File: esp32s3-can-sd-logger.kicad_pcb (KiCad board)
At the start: 4 copper layers, 84 x 72 mm, 162 parts, among them J1 PWR + CAN harness, J2 USB-C, J3 UART0, J4 I2C / Qwiic, J5 Spare IO, J6 Rail break-out, J7 microSD push-pull, J8 Sensor harness, Q1 100V 6.8mOhm N-ch, Q2 -20V 2.3A P-ch, Q3 60V 300mA N-ch, SW1 RESET, SW2 BOOT, U1 LM74700-Q1, U2 LM5164 (5V), U3 LM5164 (3V3), U4 ESP32-S3-WROOM-1-N16R8, U5 USBLC6-2SC6, U6 TJA1051T/3, U7 ADS1115

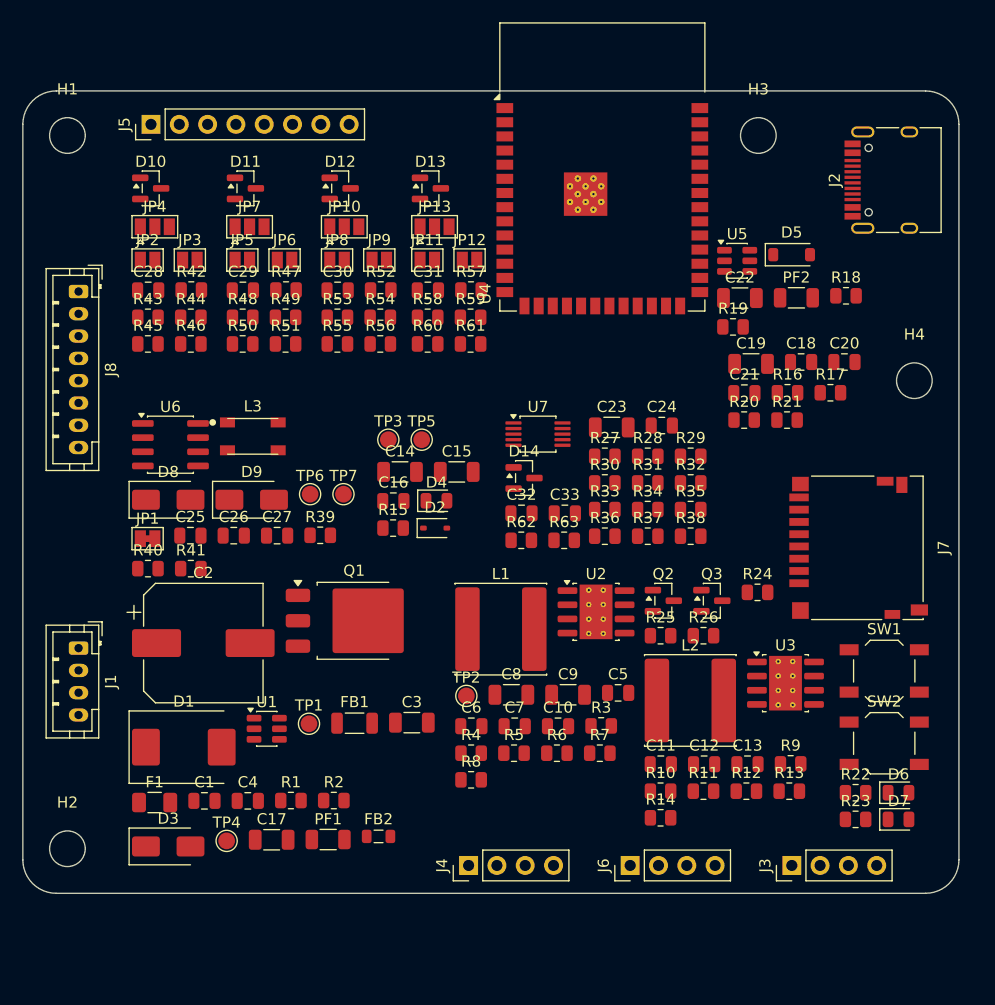
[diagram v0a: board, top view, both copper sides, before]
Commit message: Add WS2812 5V DIN, SPI breakout, and PCB handoff docs.
Shift-light header uses a 74AHCT1G125 so GPIO48 drives real 5V data; SPI lands on IO40/41/42/47 with spare IO3/45/46 kept. README §10 covers remaining routing for the next agent.

Co-authored-by: Cursor <cursoragent@cursor.com>
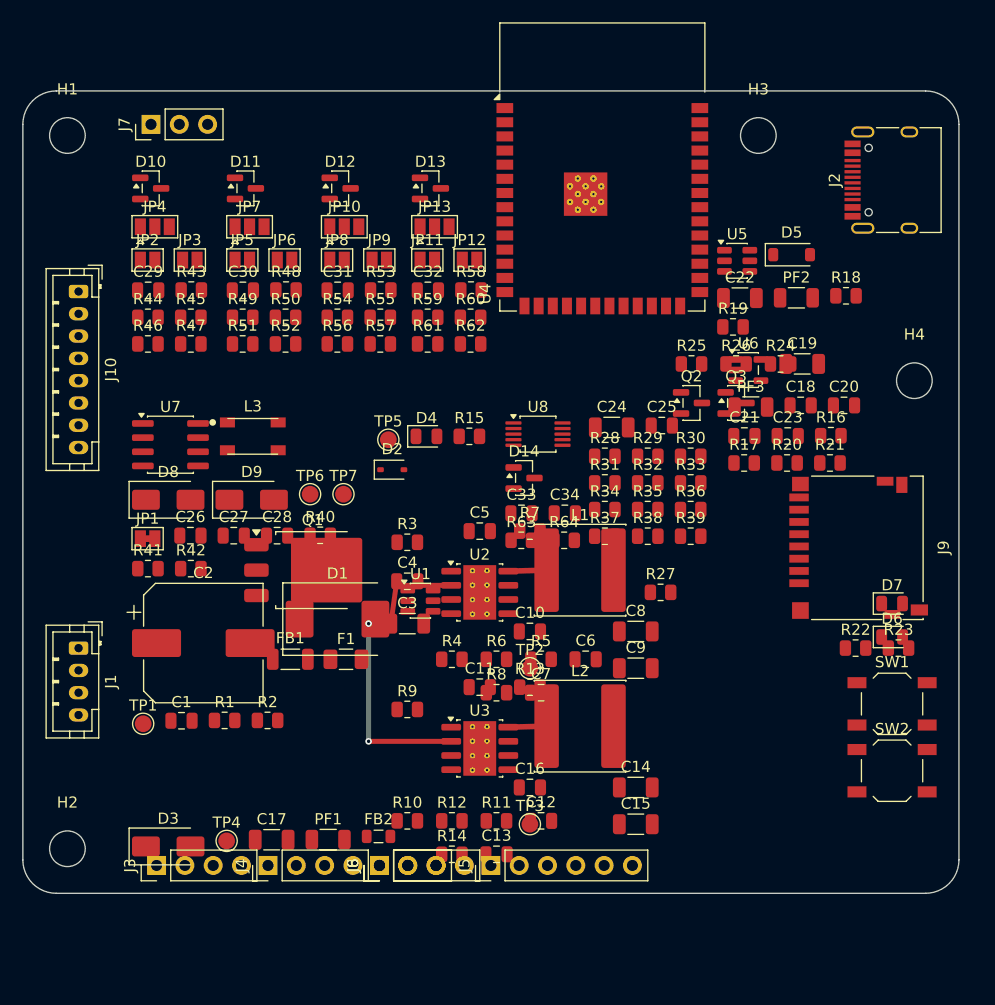
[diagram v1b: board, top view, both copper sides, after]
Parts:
- added C34: 100nF 16V, C_0805_2012Metric, F.Cu at (48.6, 37.9)
- added J10: Sensor harness, JST_PH_B8B-PH-K_1x08_P2.00mm_Vertical, F.Cu at (5.00, 18.0)
- added J9: microSD push-pull, microSD_HC_Hirose_DM3D-SF, F.Cu at (75.0, 41.0)
- added PF3: 0.5A hold, R_1206_3216Metric, F.Cu at (65.3, 28.4)
- added R64: 10k, R_0805_2012Metric, F.Cu at (48.6, 40.3)
- added U8: ADS1115, VSSOP-10_3x3mm_P0.5mm, F.Cu at (46.2, 30.8)
- C23: value 10uF 6.3V -> 100nF 16V; footprint C_1206_3216Metric -> C_0805_2012Metric
- C24: value 100nF 16V -> 10uF 6.3V; footprint C_0805_2012Metric -> C_1206_3216Metric
- C27: value 4.7nF 50V -> 100nF 16V
- C28: value 100nF 16V -> 4.7nF 50V
- J5: value Spare IO -> SPI; footprint PinHeader_1x08_P2.54mm_Vertical -> PinHeader_1x06_P2.54mm_Vertical
- J6: value Rail break-out -> WS2812; footprint PinHeader_1x04_P2.54mm_Vertical -> PinHeader_1x03_P2.54mm_Vertical
- J7: value microSD push-pull -> Spare IO; footprint microSD_HC_Hirose_DM3D-SF -> PinHeader_1x03_P2.54mm_Vertical
- J8: value Sensor harness -> Rail break-out; footprint JST_PH_B8B-PH-K_1x08_P2.00mm_Vertical -> PinHeader_1x04_P2.54mm_Vertical
- R24: value 100k -> 33
- R25, R63: value 10k -> 100k
- R26: value 100k -> 10k
- R27: value 33 -> 100k
- R33: value 47k -> 33
- R39: value 10k -> 47k
- R40: value 60.4 -> 10k
- R42: value 1k 0.1% -> 60.4
- R43, R48, R53, R58: value 2.49k -> 1k 0.1%
- R44, R49, R54, R59: value 10k 0.1% -> 2.49k
- R45, R50, R55, R60: value 15k 0.1% -> 10k 0.1%
- R46, R51, R56, R61: value 2.21k 0.1% -> 15k 0.1%
- R47, R52, R57: value 1k 0.1% -> 2.21k 0.1%
- R62: value 100k -> 2.21k 0.1%
- U6: value TJA1051T/3 -> 74AHCT1G125; footprint SOIC-8_3.9x4.9mm_P1.27mm -> SOT-23-5
- U7: value ADS1115 -> TJA1051T/3; footprint VSSOP-10_3x3mm_P0.5mm -> SOIC-8_3.9x4.9mm_P1.27mm
- moved J7 74.0 mm to (11.5, 3.00), turned to 90 degrees
- moved J5 73.2 mm to (42.0, 69.5)
- moved J8 58.1 mm to (32.0, 69.5), turned to 90 degrees
- moved J3 57.0 mm to (12.0, 69.5)
- moved U6 52.3 mm to (65.1, 25.0)
- moved C25 43.4 mm to (57.3, 30.0)
- moved TP3 36.8 mm to (45.5, 65.8)
- moved C15 35.5 mm to (55.0, 65.8)
- moved C14 35.3 mm to (55.0, 62.5)
- moved R9 34.7 mm to (34.5, 55.5)
- moved R39 33.2 mm to (59.9, 40.0)
- moved U7 33.0 mm to (13.2, 31.7)
- moved C16 28.5 mm to (45.5, 62.5)
- moved U3 28.1 mm to (41.0, 59.0)
- moved R12 26.6 mm to (38.5, 65.5)
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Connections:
- C23 pad 1: SD_VDD -> +5V
- C25 pad 1: +5V -> SD_VDD
- C26 pad 1: +3V3 -> +5V
- C27 pad 1: CAN_SPLIT -> +3V3
- C28 pad 1: AIN1 -> CAN_SPLIT
- C29 pad 1: AIN2 -> AIN1
- C30 pad 1: AIN3 -> AIN2
- C31 pad 1: AIN4 -> AIN3
- C32 pad 1: +3V3 -> AIN4
- C33 pad 1: VBAT_SNS -> +3V3
- J5 pad 1: IO3 -> +3V3
- J5 pad 2: IO45 -> GND
- J5 pad 3: IO46 -> SPI_SCK
- J5 pad 4: IO47 -> SPI_MISO
- J5 pad 5: IO48 -> SPI_MOSI
- J5 pad 6: IO40 -> SPI_CS
- J6 pad 1: +5V -> LED_5V
- J6 pad 2: +3V3 -> LED_DIN
- J7 pad 1: SD_D2_C -> IO3
- J7 pad 2: SD_D3_C -> IO45
- J7 pad 3: SD_CMD_C -> IO46
- J8 pad 1: +5VS -> +5V
- J8 pad 2: AIN1_IN -> +3V3
- J8 pad 3: AIN2_IN -> GND
- J8 pad 4: AIN3_IN -> GND
- R24 pad 1: +3V3 -> LED_DIN_MCU
- R24 pad 2: SD_PG -> LED_DIN_A
- R25 pad 1: SD_PWR_EN -> +3V3
- R25 pad 2: SD_EN_G -> SD_PG
- R26 pad 1: SD_EN_G -> SD_PWR_EN
- R26 pad 2: GND -> SD_EN_G
- R27 pad 1: SD_CLK -> SD_EN_G
- R27 pad 2: SD_CLK_C -> GND
- R28 pad 1: SD_CMD -> SD_CLK
- R28 pad 2: SD_CMD_C -> SD_CLK_C
- R29 pad 1: SD_D0 -> SD_CMD
- R29 pad 2: SD_D0_C -> SD_CMD_C
- R30 pad 1: SD_D1 -> SD_D0
- R30 pad 2: SD_D1_C -> SD_D0_C
- R31 pad 1: SD_D2 -> SD_D1
- R31 pad 2: SD_D2_C -> SD_D1_C
- R32 pad 1: SD_D3 -> SD_D2
- R32 pad 2: SD_D3_C -> SD_D2_C
- R33 pad 1: SD_VDD -> SD_D3
- R33 pad 2: SD_CMD_C -> SD_D3_C
- R34 pad 2: SD_D0_C -> SD_CMD_C
- R35 pad 2: SD_D1_C -> SD_D0_C
- R36 pad 2: SD_D2_C -> SD_D1_C
- R37 pad 2: SD_D3_C -> SD_D2_C
- R38 pad 1: +3V3 -> SD_VDD
- R38 pad 2: SD_CD -> SD_D3_C
- R39 pad 1: CAN_S -> +3V3
- R39 pad 2: GND -> SD_CD
- R40 pad 1: TERM_A -> CAN_S
- R40 pad 2: CAN_SPLIT -> GND
- R41 pad 1: CAN_SPLIT -> TERM_A
- R41 pad 2: CAN_L -> CAN_SPLIT
- R42 pad 1: AIN1_IN -> CAN_SPLIT
- R42 pad 2: AIN1_A -> CAN_L
- R43 pad 1: AIN1_PU -> AIN1_IN
- R44 pad 1: AIN1_A -> AIN1_PU
- R44 pad 2: AIN1 -> AIN1_A
- R45 pad 1: AIN1_R1 -> AIN1_A
- R45 pad 2: GND -> AIN1
- R46 pad 1: AIN1_R2 -> AIN1_R1
- R47 pad 1: AIN2_IN -> AIN1_R2
- R47 pad 2: AIN2_A -> GND
- R48 pad 1: AIN2_PU -> AIN2_IN
- R49 pad 1: AIN2_A -> AIN2_PU
- R49 pad 2: AIN2 -> AIN2_A
- R50 pad 1: AIN2_R1 -> AIN2_A
- R50 pad 2: GND -> AIN2
- R51 pad 1: AIN2_R2 -> AIN2_R1
- R52 pad 1: AIN3_IN -> AIN2_R2
- R52 pad 2: AIN3_A -> GND
- R53 pad 1: AIN3_PU -> AIN3_IN
- R54 pad 1: AIN3_A -> AIN3_PU
- R54 pad 2: AIN3 -> AIN3_A
- R55 pad 1: AIN3_R1 -> AIN3_A
- R55 pad 2: GND -> AIN3
- R56 pad 1: AIN3_R2 -> AIN3_R1
- R57 pad 1: AIN4_IN -> AIN3_R2
- R57 pad 2: AIN4_A -> GND
- R58 pad 1: AIN4_PU -> AIN4_IN
- R59 pad 1: AIN4_A -> AIN4_PU
- R59 pad 2: AIN4 -> AIN4_A
- R60 pad 1: AIN4_R1 -> AIN4_A
- R60 pad 2: GND -> AIN4
- R61 pad 1: AIN4_R2 -> AIN4_R1
- R62 pad 1: +VBAT -> AIN4_R2
- R62 pad 2: VBAT_SNS -> GND
- R63 pad 1: VBAT_SNS -> +VBAT
- R63 pad 2: GND -> VBAT_SNS
- U4 pad 24: IO47 -> SPI_CS
- U4 pad 25: IO48 -> LED_DIN_MCU
- U4 pad 33: IO40 -> SPI_SCK
- U4 pad 34: IO41 -> SPI_MISO
- U4 pad 35: IO42 -> SPI_MOSI
- U6 pad 1: CAN_TX -> GND
- U6 pad 2: GND -> LED_DIN_A
- U6 pad 3: +5V -> GND
- U6 pad 4: CAN_RX -> LED_DIN
- U6 pad 5: +3V3 -> +5V
- U7 pad 1: GND -> CAN_TX
- U7 pad 2: (no net) -> GND
- U7 pad 3: GND -> +5V
- U7 pad 4: AIN1 -> CAN_RX
- U7 pad 5: AIN2 -> +3V3
- U7 pad 6: AIN3 -> CANL_T
- U7 pad 7: AIN4 -> CANH_T
- U7 pad 8: +3V3 -> CAN_S
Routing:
- net +VBAT: track 0.00 -> 29.1 mm, vias 0 -> 2
- net SW_5V: track 0.00 -> 3.44 mm
- net SW_3V3: track 0.00 -> 3.44 mm

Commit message: Reconcile placement ownership: generate_pcb places, route_bucks routes
The board generator and route_bucks.py both placed the buck parts and
fought each other -- 180 DRC violations of stacked pads and courtyards.
Now generate_pcb.py owns all placement: the two LM5164 islands are in a
BUCK_FIXED table keyed by (sheet, value, exact net set), so reference
renumbering can never scatter them again, and their geometry is
redesigned against real courtyard sizes (EN/BST/ramp row, IC+inductor
row with input caps rotated toward the VIN pin, RON/FB row, ripple/PG
row, output caps at the inductor).

route_bucks.py is routing-only: it finds parts on the saved board by
value/net signature and draws the SW loops plus the +VBAT feed, dropping
to B.Cu between the resistor rows.

The new WS2812/SPI circuitry gets placed too: SPI header on the top
edge, WS2812 header on the bottom edge next to its AHCT buffer strip,
LEDs and buttons at the right edge, board grown to 84 x 74 mm.

kicad-cli pcb drc: zero violations. Schematic validation still clean.

Co-Authored-By: Claude Fable 5 <noreply@anthropic.com>
Claude-Session: https://claude.ai/code/session_01DhNbL25h25p8VFCjRfJik9
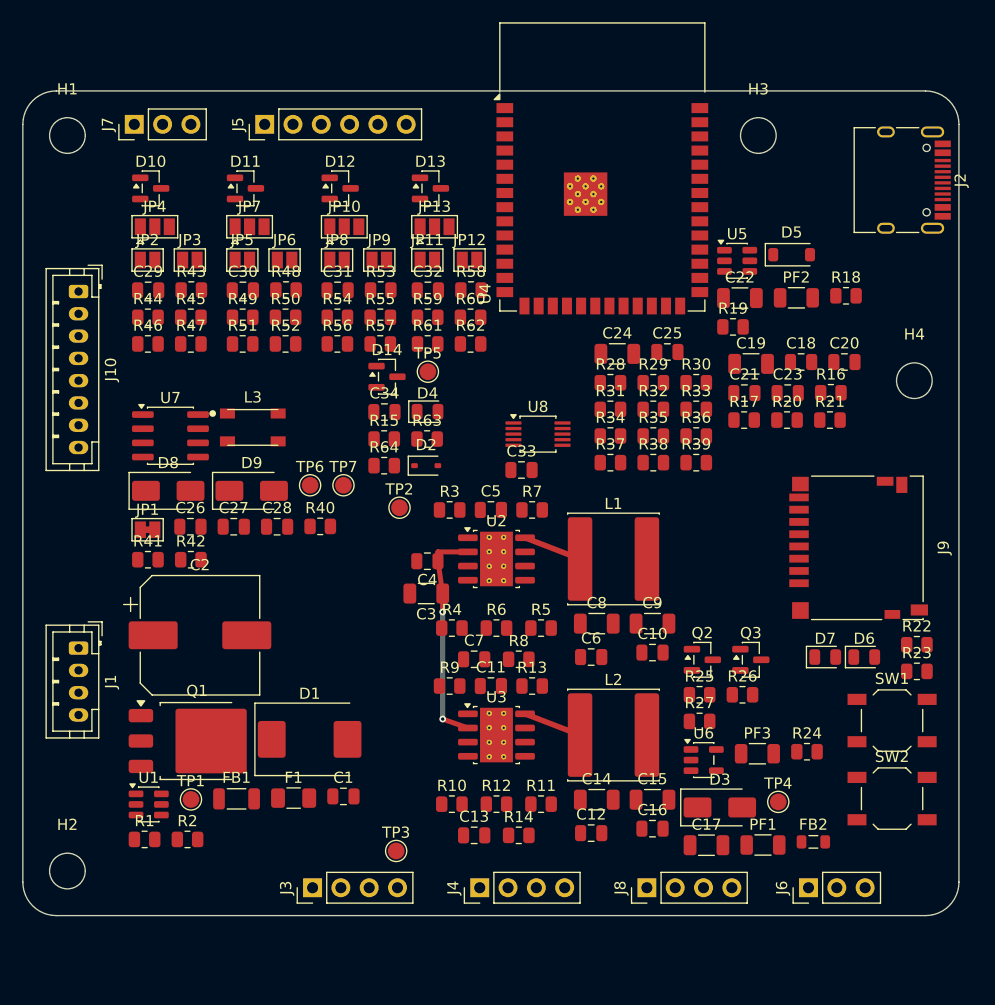
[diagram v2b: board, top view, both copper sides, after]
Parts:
- moved J5 69.5 mm to (21.7, 3.00)
- moved D3 49.6 mm to (62.5, 64.3)
- moved TP4 49.6 mm to (67.8, 63.8)
- moved FB2 39.0 mm to (70.9, 67.4)
- moved PF1 39.0 mm to (66.4, 67.7)
- moved C17 39.0 mm to (61.3, 67.7)
- moved J6 38.6 mm to (70.5, 71.5)
- moved U6 35.2 mm to (61.1, 60.0)
- moved R24 34.9 mm to (70.4, 59.3)
- moved PF3 31.1 mm to (65.9, 59.5)
- moved U1 30.5 mm to (11.3, 64.0)
- moved R25 29.7 mm to (60.7, 54.2)
- moved R26 29.7 mm to (64.6, 54.2)
- moved J8 24.1 mm to (56.0, 71.5)
- moved Q3 23.1 mm to (65.3, 51.0)
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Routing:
- net +VBAT: track 29.1 -> 20.1 mm
- net SW_5V: track 3.44 -> 5.29 mm
- net SW_3V3: track 3.44 -> 5.29 mm
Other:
- board size 84 x 72 mm -> 84 x 74 mm

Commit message: Add the routing pipeline: plane stitching, plane-safe DSN, fab export
Routing the board turned out to hinge on two things the obvious approach
gets wrong, so both are now encoded in scripts rather than lore:

- KiCad exports every copper layer to Specctra as `signal`, so the
  autorouter ran IO45 and SPI_MOSI straight across the middle of the
  +3V3 pour, fragmenting it and orphaning everything that depended on
  the plane. gen/export_dsn.py rewrites In1/In2 as `power` so routing
  stays on F.Cu/B.Cu.
- A pad on GND or +3V3 wants a via to its plane, not a routed track.
  gen/stitch_planes.py places all 117 of them before routing, so the
  router sees them as obstacles and has only signals left to solve. It
  uses real point-to-rectangle and point-to-segment distances; bounding
  boxes are far too pessimistic in a dense field and refuse room that is
  really there. It also reads pad geometry from the bounding box rather
  than GetSize(), which is in the footprint's own frame and comes out
  transposed for a rotated connector.

Also new: gen/import_ses.py (session import + zone refill),
gen/finish_routing.py (ties duplicated connector pins such as USB-C D+
on A6/B6, reports leftovers), gen/export_fab.py (Gerbers, drill, JLC
assembly BOM and position files), and gen/build_board.py which drives
the whole chain in one command.

Placement changes: a 0.6 mm rule-area band around the perimeter so the
autorouter honours copper-to-edge clearance, solid plane connections for
through-hole plane pads and the LM5164 exposed pads (starved thermal
spokes otherwise), and the USB-C receptacle moved ~2.5 mm inboard so its
A/B duplicate pins have a via channel to be tied in.

Co-Authored-By: Claude Fable 5 <noreply@anthropic.com>
Claude-Session: https://claude.ai/code/session_01DhNbL25h25p8VFCjRfJik9
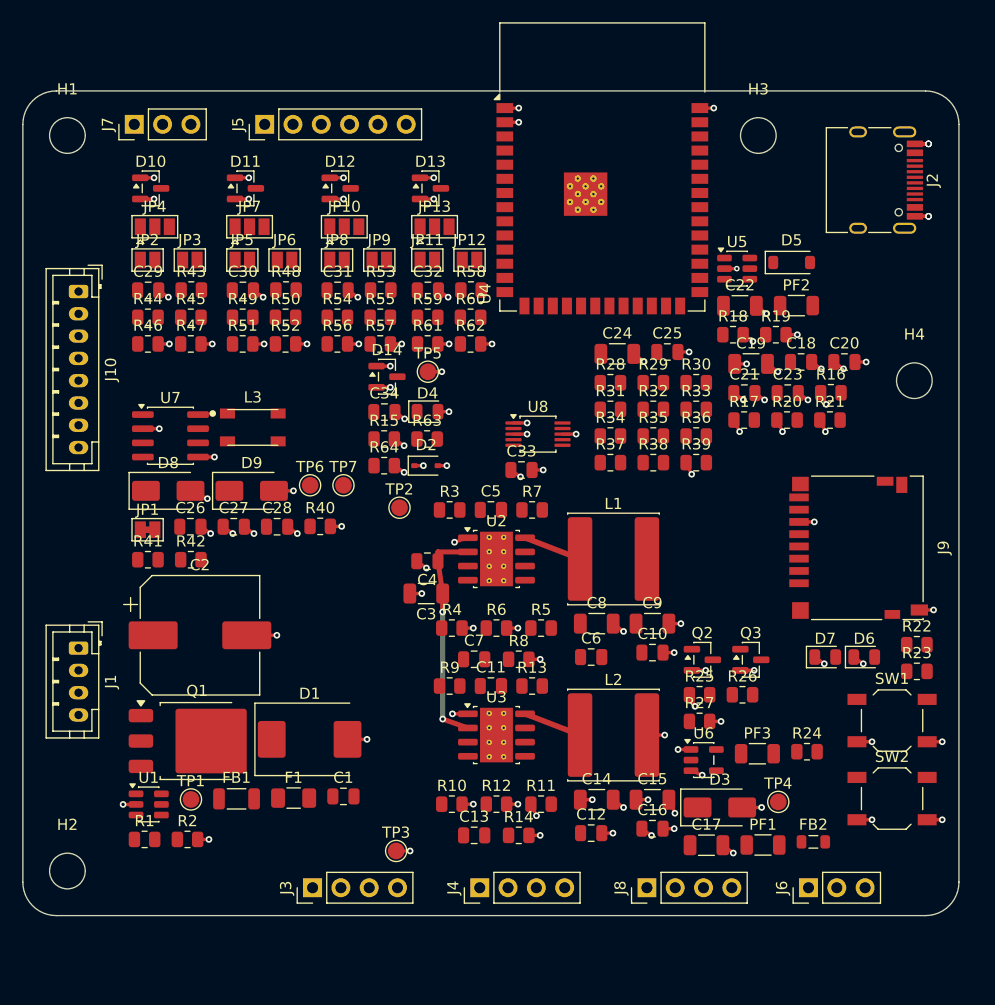
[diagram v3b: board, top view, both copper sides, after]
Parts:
- moved R18 10.7 mm to (63.7, 21.9)
- moved R19 3.91 mm to (67.6, 21.9)
- moved J2 2.50 mm to (76.0, 8.00)
- moved U5 0.70 mm to (64.1, 15.9)
- moved D5 0.70 mm to (69.0, 15.4)
- moved C22 0.70 mm to (64.3, 19.3)
- moved PF2 0.70 mm to (69.4, 19.3)
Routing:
- net GND: track 0.00 -> 95.3 mm, vias 0 -> 81
- net +3V3: track 0.00 -> 35.7 mm, vias 0 -> 31
